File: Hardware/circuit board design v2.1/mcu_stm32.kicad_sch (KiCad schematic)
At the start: 35 parts, among them J1 Conn_01x02_Male, J4 U.FL-R-SMT-1_10_, J6 Conn_01x02_Male, U1 STM32F446RETx, U10 LAMBDA-9D, U11 2SCR512R_HZG, U2 W25Q64JVSS, U3 SDR08540M3-01, Y1 ECS-80-8-33Q-ADS-TR3

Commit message: Found error transistor pinout
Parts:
- R6: value R_0603 -> 3.3k
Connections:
- net GND: now also U11.2 (E); no longer U11.1 (E)
- net GPS_reset: now also U1.52 (PC11); no longer U1.55 (PB3)
- net OSCI+: now reaches C17.1, U1.5 (PH0), Y1.1
- net OSCI-: now reaches C18.1, U1.6 (PH1), Y1.3
- net at R6.2: now also U11.1 (B); no longer U11.2 (B)
- no-connect marks 29 -> 32
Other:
- moved on the sheet: R6
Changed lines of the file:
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@@
   (no_connect (at 167.64 130.81))
   (no_connect (at 167.64 133.35))
-  (no_connect (at 132.08 123.19))
   (no_connect (at 132.08 128.27))
   (no_connect (at 132.08 130.81))
@@
   (no_connect (at 132.08 59.69))
   (no_connect (at 132.08 54.61))
+  (no_connect (at 167.64 123.19))
+  (no_connect (at 167.64 105.41))
+  (no_connect (at 167.64 97.79))
+  (no_connect (at 167.64 100.33))
   (wire (pts (xy 175.26 33.02) (xy 175.26 29.21))
     (stroke (width 0) (type default) (color 0 0 0 0))
@@
     (stroke (width 0) (type default) (color 0 0 0 0))
   )
+  (wire (pts (xy 121.92 123.19) (xy 132.08 123.19))
+    (stroke (width 0) (type default) (color 0 0 0 0))
+  )
   (wire (pts (xy 147.32 143.51) (xy 149.86 143.51))
     (stroke (width 0) (type default) (color 0 0 0 0))
@@
     (stroke (width 0) (type default) (color 0 0 0 0))
   )
-  (wire (pts (xy 220.98 143.51) (xy 228.6 143.51))
+  (wire (pts (xy 227.33 143.51) (xy 228.6 143.51))
     (stroke (width 0) (type default) (color 0 0 0 0))
   )
@@
     (stroke (width 0) (type default) (color 0 0 0 0))
   )
-  (wire (pts (xy 209.55 143.51) (xy 215.9 143.51))
+  (wire (pts (xy 215.9 143.51) (xy 222.25 143.51))
     (stroke (width 0) (type default) (color 0 0 0 0))
   )
@@
   )
   (wire (pts (xy 248.92 105.41) (xy 248.92 107.95))
-    (stroke (width 0) (type default) (color 0 0 0 0))
-  )
-  (wire (pts (xy 167.64 105.41) (xy 173.99 105.41))
     (stroke (width 0) (type default) (color 0 0 0 0))
   )
@@
     (effects (font (size 1.27 1.27)) (justify left bottom))
   )
-  (label "buzzer_gate" (at 209.55 143.51 180)
+  (label "buzzer_gate" (at 215.9 143.51 180)
     (effects (font (size 1.27 1.27)) (justify right bottom))
   )
@@
     (effects (font (size 1.27 1.27)) (justify left bottom))
   )
+  (label "OSCI-" (at 105.41 85.09 0)
+    (effects (font (size 1.27 1.27)) (justify left bottom))
+  )
   (label "buzzer_gate" (at 173.99 62.23 0)
     (effects (font (size 1.27 1.27)) (justify left bottom))
@@
     (effects (font (size 1.27 1.27)) (justify right bottom))
   )
+  (label "OSCI+" (at 90.17 82.55 0)
+    (effects (font (size 1.27 1.27)) (justify left bottom))
+  )
   (label "Radio_TX" (at 48.26 170.18 180)
     (effects (font (size 1.27 1.27)) (justify right bottom))
@@
     (effects (font (size 1.27 1.27)) (justify left))
   )
-  (hierarchical_label "GPS_reset" (shape output) (at 173.99 105.41 0)
-    (effects (font (size 1.27 1.27)) (justify left))
+  (hierarchical_label "GPS_reset" (shape output) (at 121.92 123.19 180)
+    (effects (font (size 1.27 1.27)) (justify right))
   )
   (hierarchical_label "SDA" (shape bidirectional) (at 196.85 115.57 0)
@@
     (pin "1")
   )
-  (symbol (lib_id "Components:R_0603") (at 218.44 143.51 90) (unit 1)
-    (in_bom yes) (on_board yes) (fields_autoplaced)
-    (property "Reference" "R6" (id 0) (at 218.44 137.16 90))
-    (property "Value" "R_0603" (id 1) (at 218.44 139.7 90))
-    (property "Footprint" "Components:R_0603_1608Metric" (id 2) (at 218.44 143.51 0)
-      (effects (font (size 1.27 1.27)) hide)
-    )
-    (property "Datasheet" "~" (id 3) (at 218.44 143.51 0)
-      (effects (font (size 1.27 1.27)) hide)
-    )
+  (symbol (lib_id "Components:R_0603") (at 224.79 143.51 90) (unit 1)
+    (in_bom yes) (on_board yes) (fields_autoplaced)
+    (property "Reference" "R6" (id 0) (at 224.79 137.16 90))
+    (property "Value" "3.3k" (id 1) (at 224.79 139.7 90))
+    (property "Footprint" "Components:R_0603_1608Metric" (id 2) (at 224.79 143.51 0)
+      (effects (font (size 1.27 1.27)) hide)
+    )
+    (property "Datasheet" "~" (id 3) (at 224.79 143.51 0)
+      (effects (font (size 1.27 1.27)) hide)
+    )

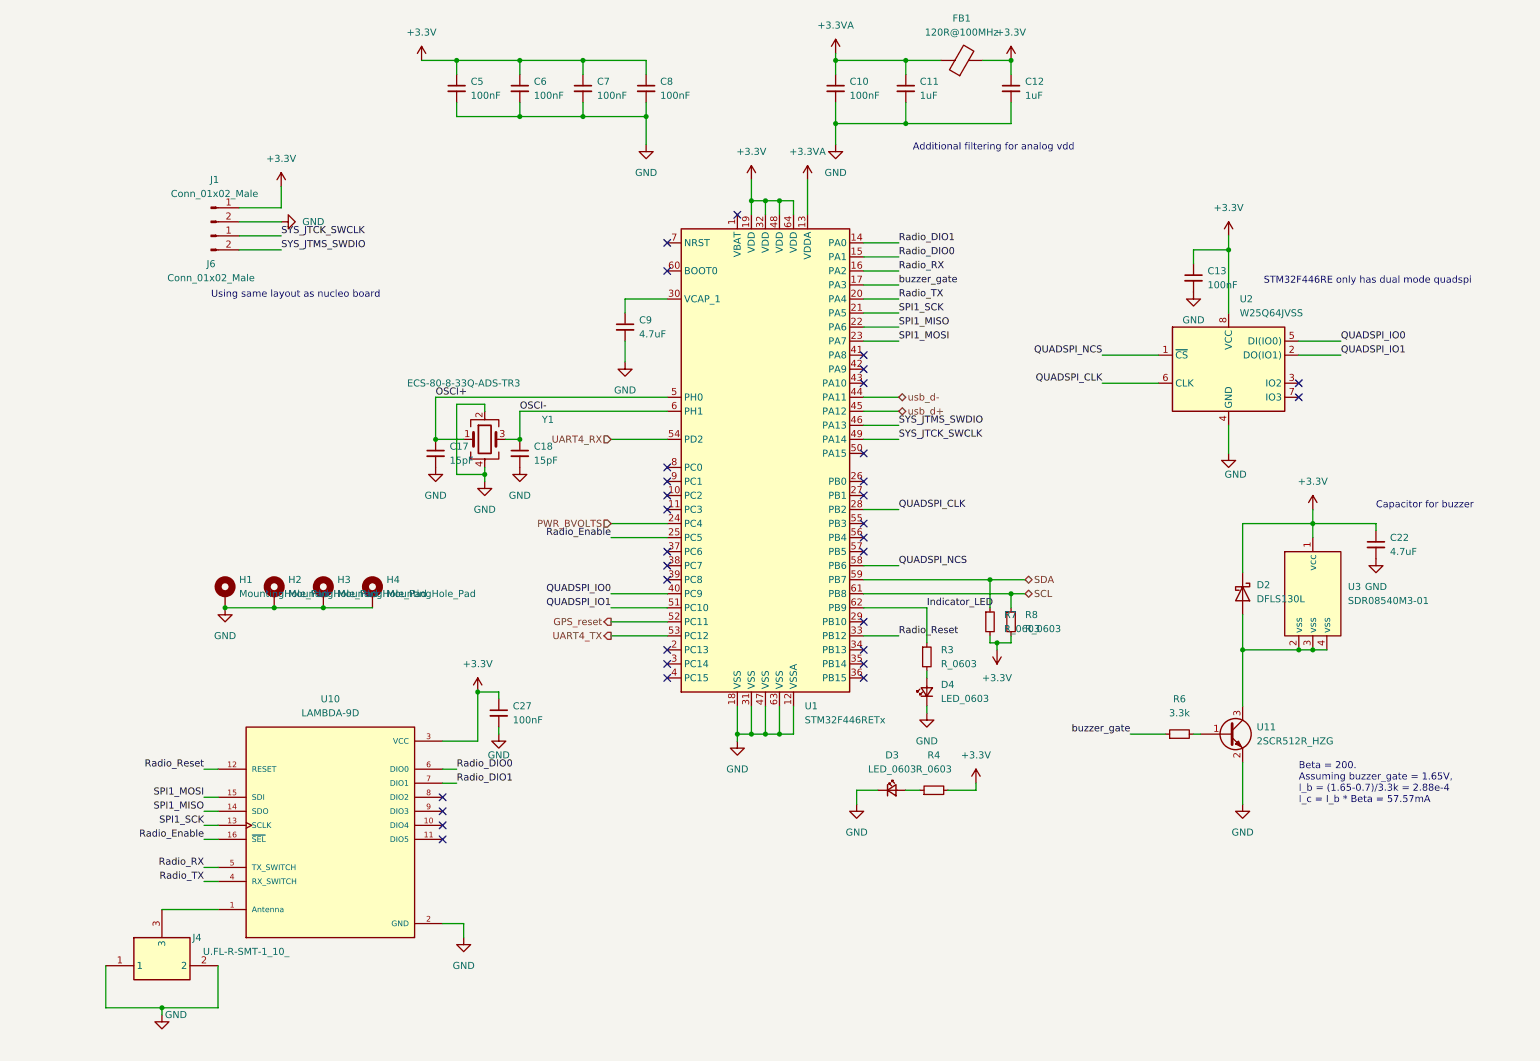
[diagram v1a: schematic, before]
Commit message: Renamed pins in stm32cubeide and finished routing for V2.1
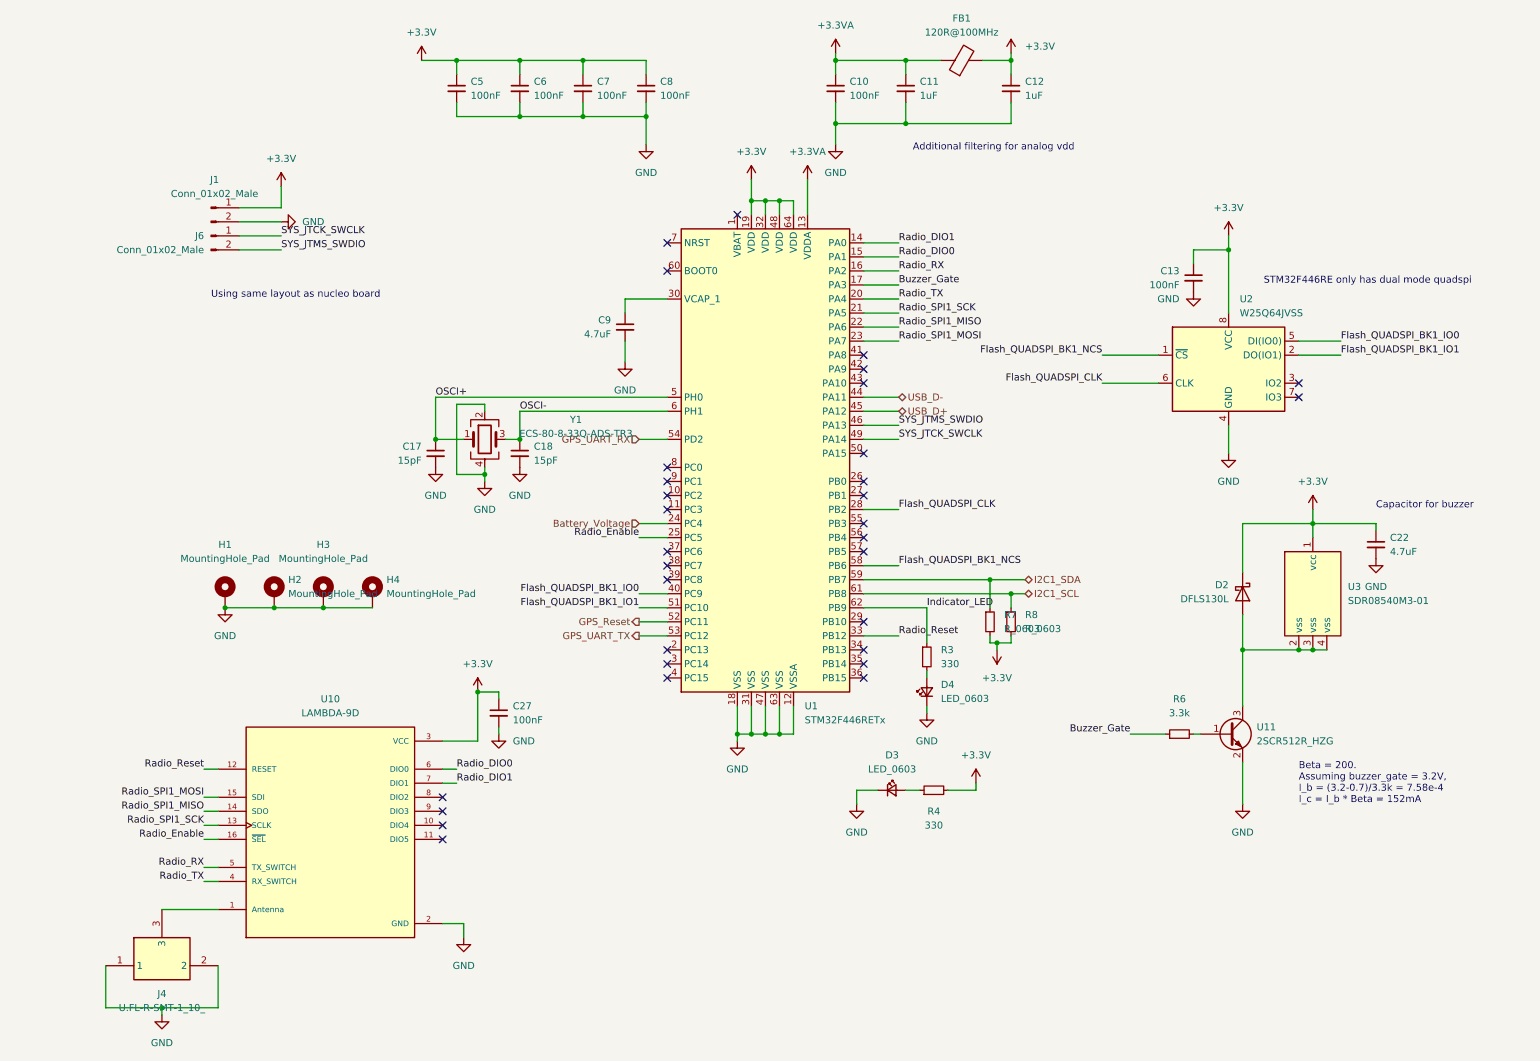
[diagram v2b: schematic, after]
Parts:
- R3, R4: value R_0603 -> 330
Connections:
- net GPS_reset renamed GPS_Reset
- net PWR_BVOLTS renamed Battery_Voltage
- net QUADSPI_CLK renamed Flash_QUADSPI_CLK
- net QUADSPI_IO0 renamed Flash_QUADSPI_BK1_IO0
- net QUADSPI_IO1 renamed Flash_QUADSPI_BK1_IO1
- net QUADSPI_NCS renamed Flash_QUADSPI_BK1_NCS
- net SCL renamed I2C1_SCL
- net SDA renamed I2C1_SDA
- net SPI1_MISO renamed Radio_SPI1_MISO
- net SPI1_MOSI renamed Radio_SPI1_MOSI
- net SPI1_SCK renamed Radio_SPI1_SCK
- net UART4_RX renamed GPS_UART_RX
- net UART4_TX renamed GPS_UART_TX
- net buzzer_gate renamed Buzzer_Gate
- net usb_d+ renamed USB_D+
- net usb_d- renamed USB_D-
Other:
- note added: "Beta = 200. Assuming buzzer_gate = 3.2V, I_b = (3.2-0.7)/3.3k = 7.58e-4 I_c = I_b * Beta = 152mA"
- note removed: "Beta = 200. Assuming buzzer_gate = 1.65V, I_b = (1.65-0.7)/3.3k = 2.88e-4 I_c = I_b * Beta = 57.57mA"

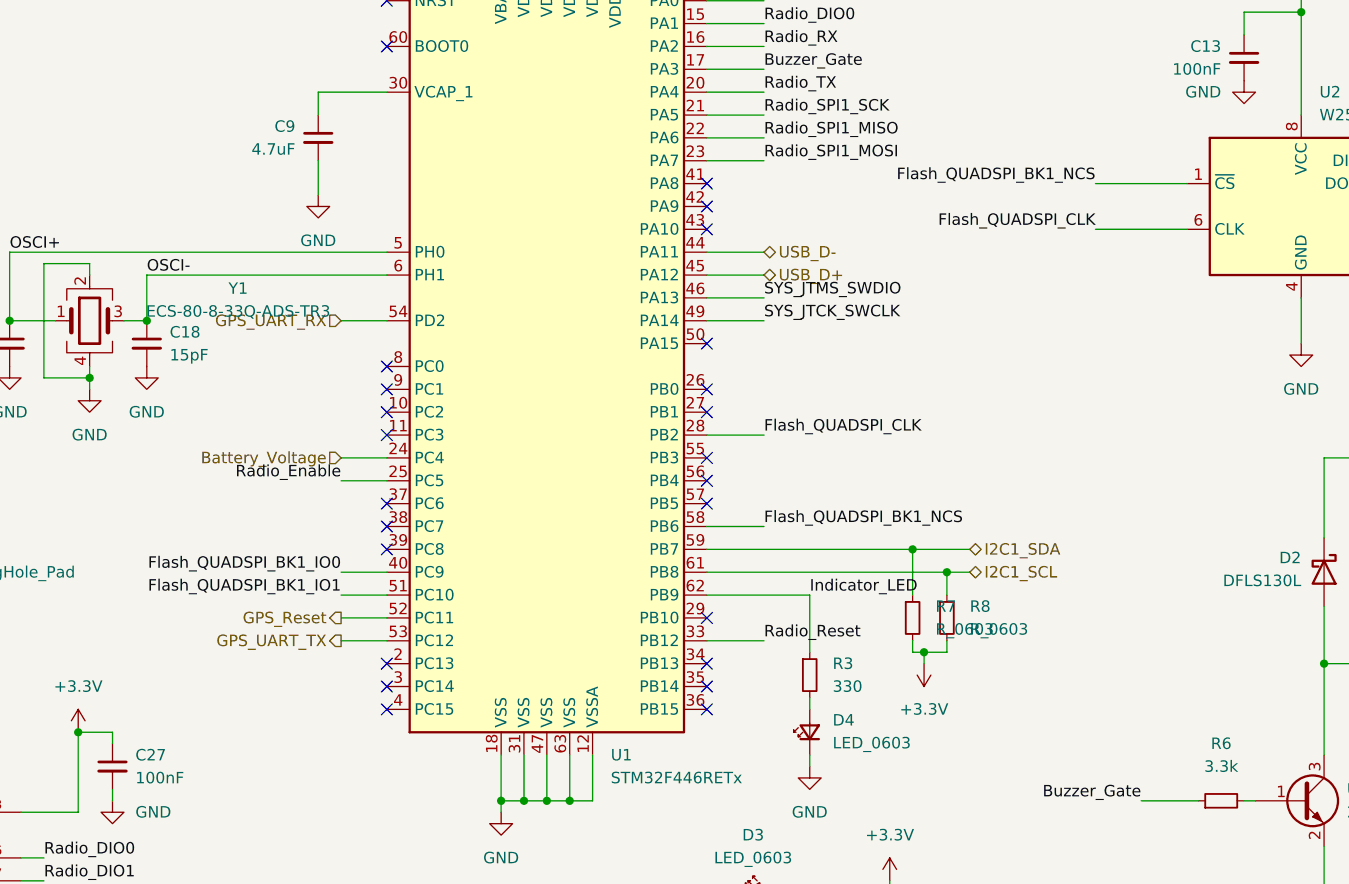
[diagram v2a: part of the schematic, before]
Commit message: Added interupt pins to from BMI088 and LIS
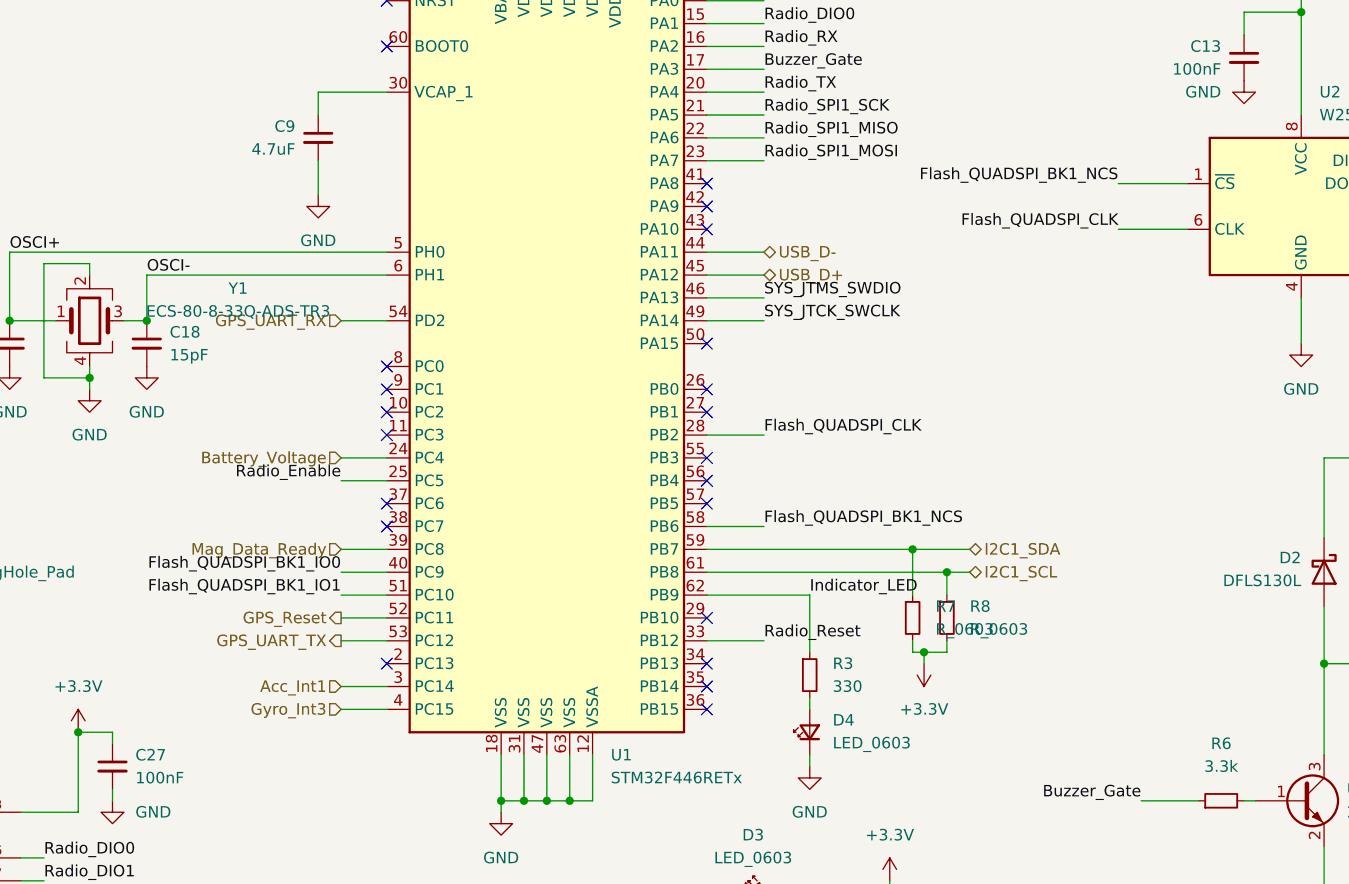
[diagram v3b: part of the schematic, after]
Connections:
- net Acc_Int1: now reaches U1.3 (PC14)
- net Mag_Data_Ready: now reaches U1.39 (PC8)
- net Gyro_Int3: now reaches U1.4 (PC15)
- no-connect marks 32 -> 29
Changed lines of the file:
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@@
   (no_connect (at 132.08 110.49))
   (no_connect (at 132.08 113.03))
-  (no_connect (at 132.08 115.57))
   (no_connect (at 167.64 128.27))
   (no_connect (at 167.64 130.81))
   (no_connect (at 167.64 133.35))
   (no_connect (at 132.08 128.27))
-  (no_connect (at 132.08 130.81))
-  (no_connect (at 132.08 133.35))
   (no_connect (at 91.44 154.94))
   (no_connect (at 91.44 157.48))
@@
     (stroke (width 0) (type default) (color 0 0 0 0))
   )
+  (wire (pts (xy 127 115.57) (xy 132.08 115.57))
+    (stroke (width 0) (type default) (color 0 0 0 0))
+  )
   (wire (pts (xy 54.61 55.88) (xy 62.23 55.88))
     (stroke (width 0) (type default) (color 0 0 0 0))
@@
     (stroke (width 0) (type default) (color 0 0 0 0))
   )
-  (wire (pts (xy 210.82 74.93) (xy 220.98 74.93))
+  (wire (pts (xy 213.36 74.93) (xy 220.98 74.93))
     (stroke (width 0) (type default) (color 0 0 0 0))
   )
@@
     (stroke (width 0) (type default) (color 0 0 0 0))
   )
-  (wire (pts (xy 210.82 80.01) (xy 220.98 80.01))
+  (wire (pts (xy 213.36 80.01) (xy 220.98 80.01))
     (stroke (width 0) (type default) (color 0 0 0 0))
   )
@@
   )
   (wire (pts (xy 50.8 185.42) (xy 50.8 193.04))
+    (stroke (width 0) (type default) (color 0 0 0 0))
+  )
+  (wire (pts (xy 127 133.35) (xy 132.08 133.35))
+    (stroke (width 0) (type default) (color 0 0 0 0))
+  )
+  (wire (pts (xy 127 130.81) (xy 132.08 130.81))
     (stroke (width 0) (type default) (color 0 0 0 0))
   )
@@
     (effects (font (size 1.27 1.27)) (justify right bottom))
   )
-  (label "Flash_QUADSPI_CLK" (at 210.82 80.01 180)
+  (label "Flash_QUADSPI_CLK" (at 213.36 80.01 180)
     (effects (font (size 1.27 1.27)) (justify right bottom))
   )
@@
     (effects (font (size 1.27 1.27)) (justify right bottom))
   )
-  (label "Flash_QUADSPI_BK1_NCS" (at 210.82 74.93 180)
+  (label "Flash_QUADSPI_BK1_NCS" (at 213.36 74.93 180)
     (effects (font (size 1.27 1.27)) (justify right bottom))
   )
@@
     (effects (font (size 1.27 1.27)) (justify left))
   )
+  (hierarchical_label "Gyro_Int3" (shape input) (at 127 133.35 180)
+    (effects (font (size 1.27 1.27)) (justify right))
+  )
+  (hierarchical_label "Acc_Int1" (shape input) (at 127 130.81 180)
+    (effects (font (size 1.27 1.27)) (justify right))
+  )
   (hierarchical_label "GPS_UART_TX" (shape output) (at 127 125.73 180)
     (effects (font (size 1.27 1.27)) (justify right))
@@
     (effects (font (size 1.27 1.27)) (justify left))
   )
+  (hierarchical_label "Mag_Data_Ready" (shape input) (at 127 115.57 180)
+    (effects (font (size 1.27 1.27)) (justify right))
+  )
   (symbol (lib_id "power:+3.3V") (at 62.23 44.45 0) (unit 1)
